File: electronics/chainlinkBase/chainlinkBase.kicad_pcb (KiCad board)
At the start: 2 copper layers, 98.4 x 190.5 mm, 128 parts, among them J101 Power In, J102 RELAY, J103 Power In, J104 RS485, J105 RS485, J106 Logic Power Out, J107 UART, J108 Output, J109 Output, J110 Output, J111 Conn_01x06_Male, J112 Conn_01x06_Male, J201 CHANNEL, J301 CHANNEL, J401 CHANNEL, J501 CHANNEL, J601 CHANNEL, SW101 SW_DIP_x04, U101 AP7361C-33E, U102 TPL7407L, U103 Buck, U104 TTGO_TDisplay, U105 MCP23017_SS, U106 SN74LV1T34DBV, U107 SP485, U108 SN74LV1T34DBV, U201 INA219BxD, U202 VN7007ALH, U301 INA219BxD, U302 VN7007ALH, U401 INA219BxD, U402 VN7007ALH, U501 INA219BxD, U502 VN7007ALH, U601 INA219BxD, U602 VN7007ALH

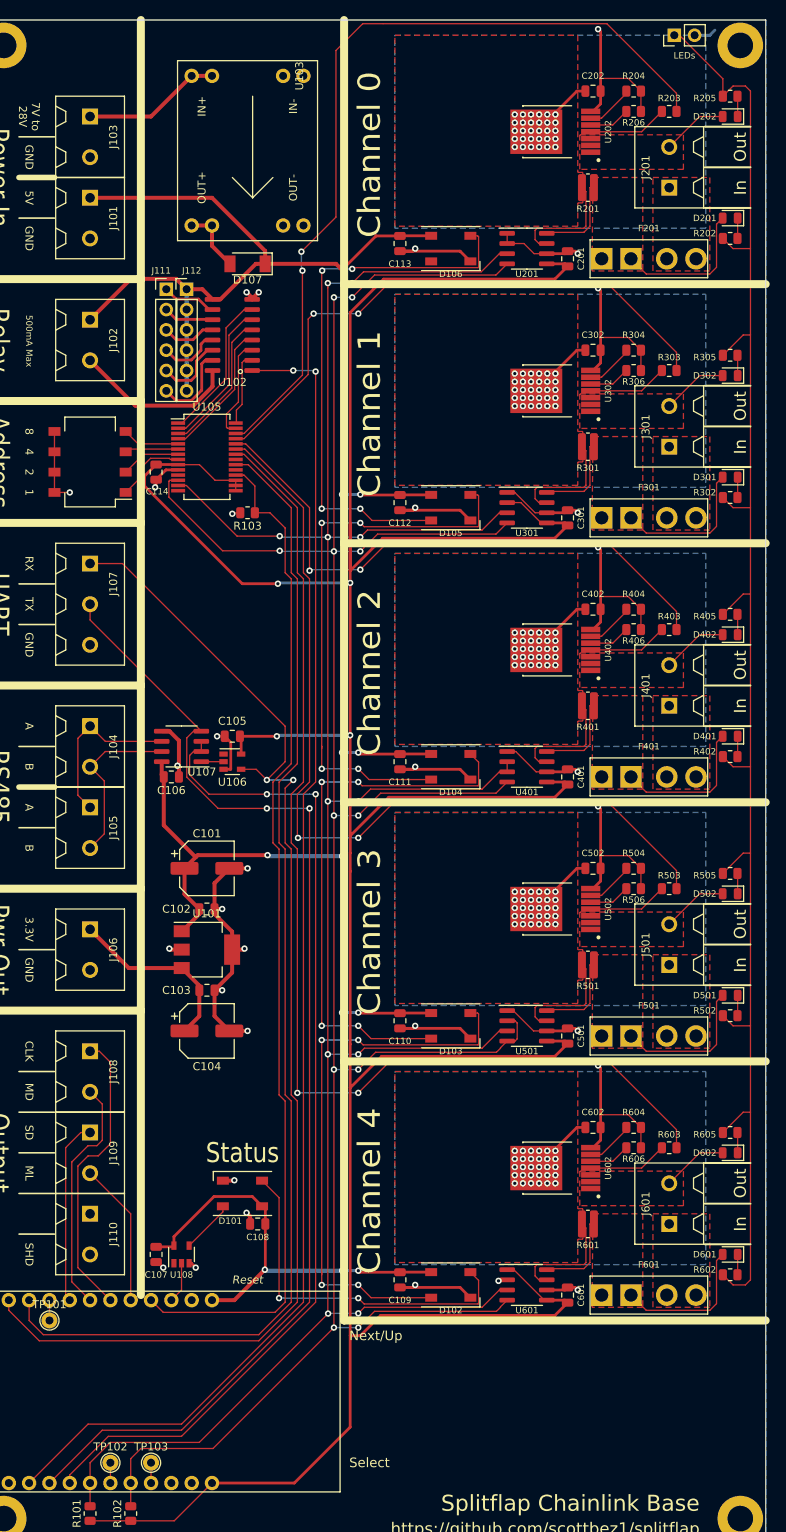
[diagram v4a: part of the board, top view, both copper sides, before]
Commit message: Layout tweaks
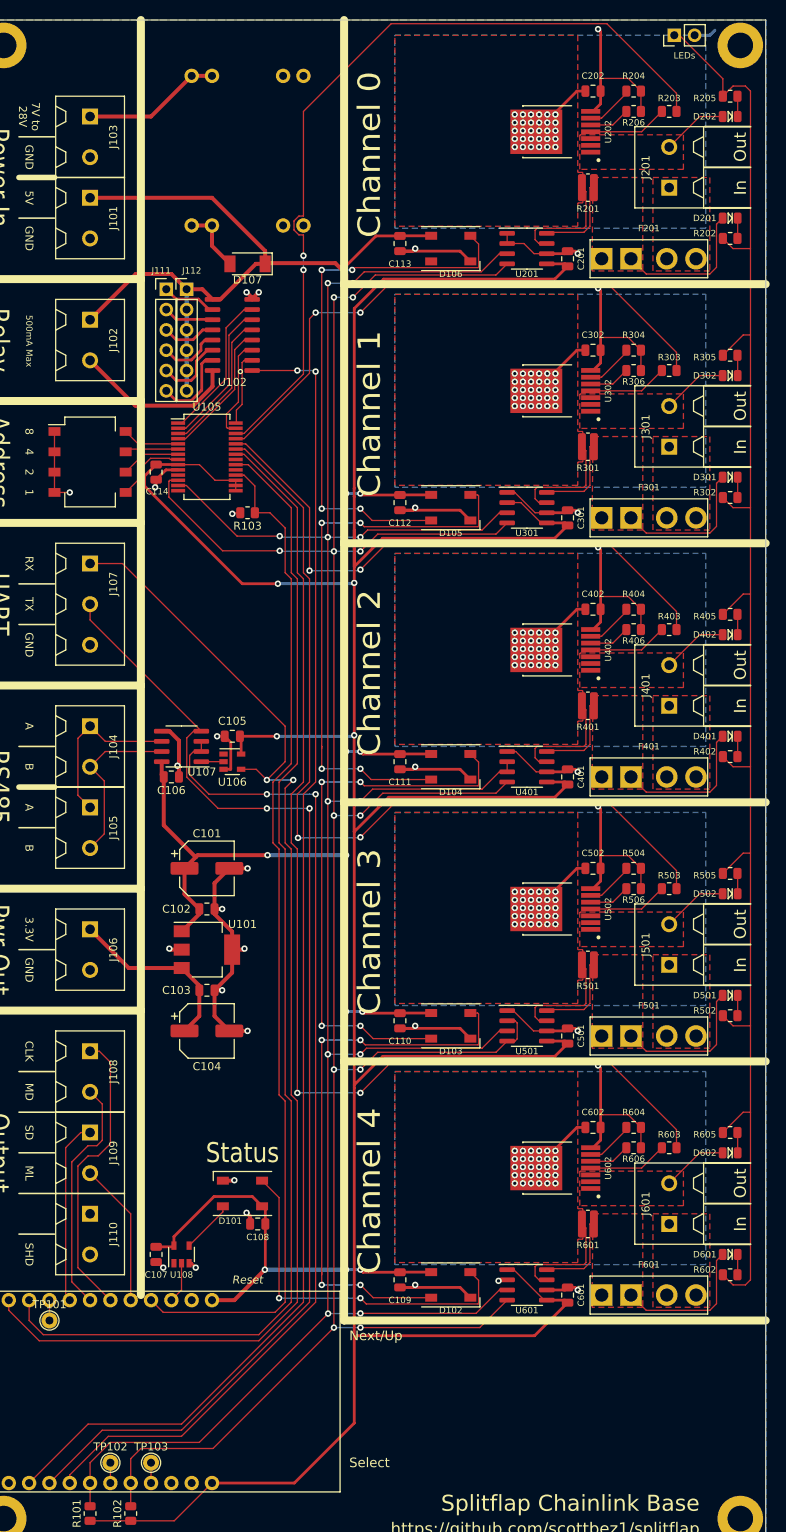
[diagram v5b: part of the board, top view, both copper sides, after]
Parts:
- D201, D202, D301, D302, D401, D402, D501, D502, D601, D602: footprint LED_SMD:LED_0805_2012Metric -> ModifiedSymbols:LED_0805_2012Metric_Silkscreen
- U103: footprint Buck:BuckModule -> Buck:BuckModuleBackSilk
- turned SW101 to 0 degrees
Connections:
- SW101 pad 1: /ADDR_0 -> GND
- SW101 pad 2: /ADDR_1 -> GND
- SW101 pad 3: /ADDR_2 -> GND
- SW101 pad 4: /ADDR_3 -> GND
- SW101 pad 5: GND -> /ADDR_0
- SW101 pad 6: GND -> /ADDR_1
- SW101 pad 7: GND -> /ADDR_2
- SW101 pad 8: GND -> /ADDR_3
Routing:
- net +5V: track 470.4 -> 345.1 mm
- net +3V3: track 418.4 -> 415.6 mm
- net /OUT0_EN: track 103.6 -> 103.1 mm

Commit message: Updates
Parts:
- JP101: footprint Connector_PinHeader_2.54mm:PinHeader_1x02_P2.54mm_Vertical -> Connector_PinHeader_2.54mm:PinHeader_1x03_P2.54mm_Vertical
- moved Z601 159.0 mm to (119.4, 186.1)
- moved Z501 122.1 mm to (119.4, 153.7)
- moved Z401 83.2 mm to (119.4, 121.3)
- moved Z301 68.0 mm to (119.4, 88.9)
- moved Z201 27.3 mm to (119.4, 56.5)
- moved JP101 2.54 mm to (114.9, 27.3), turned to 270 degrees
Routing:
- net GND: track 273.7 -> 272.2 mm
- net /LED_GND: track 200.9 -> 200.1 mm
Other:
- board text added: "off"
- board text added: "on"
